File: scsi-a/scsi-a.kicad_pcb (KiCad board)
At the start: 2 copper layers, 99.1 x 99.1 mm, 18 parts, among them J1 Conn_02x25_Odd_Even, J3 Conn_02x08_Odd_Even, J4 Conn_02x08_Odd_Even, J5 DB25_Receptacle, J6 Conn_02x10_Counter_Clockwise, J7 Conn_02x10_Counter_Clockwise, Q1 BC547, U1 Z53C80003VSG, U2 74LS138, U3 74HC00

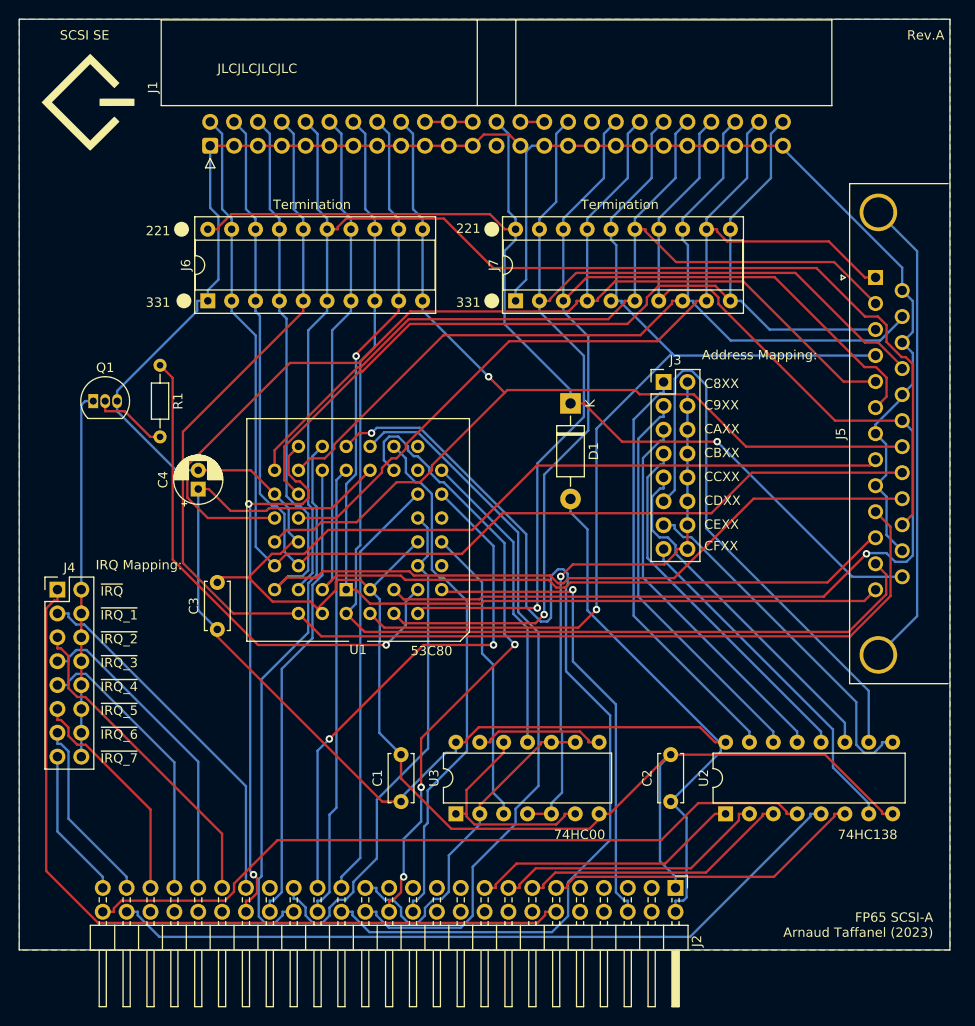
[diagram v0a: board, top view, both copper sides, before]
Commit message: Minimal change to fix SCSI CPU-Bus connection
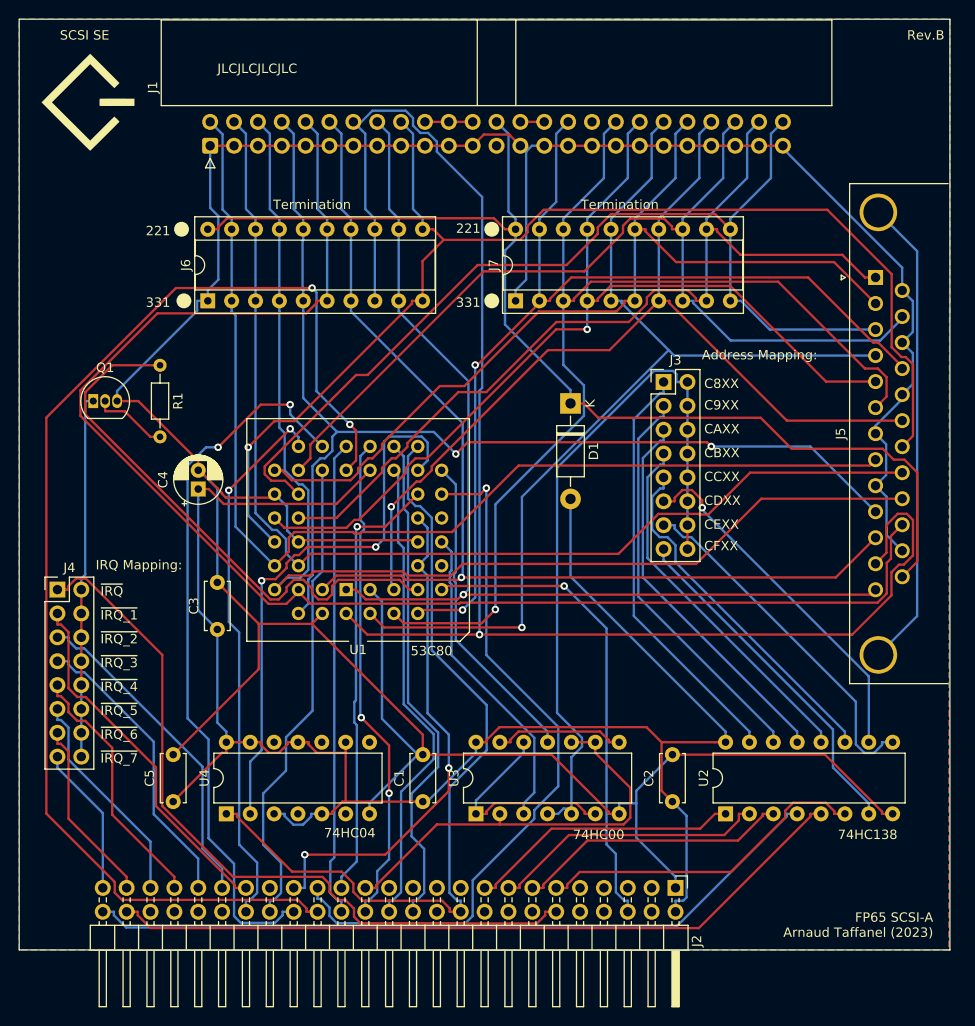
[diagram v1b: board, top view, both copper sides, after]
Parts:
- added C5: C, Capacitor_THT:C_Disc_D5.0mm_W2.5mm_P5.00mm, F.Cu at (118.0, 134.1)
- added U4: 74HC04, Package_DIP:DIP-14_W7.62mm, F.Cu at (123.6, 135.4)
- moved C1 2.32 mm to (144.6, 134.1)
- moved U3 2.13 mm to (150.2, 135.4)
- moved C2 0.18 mm to (171.1, 134.1)
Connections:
- U1 pad 18: /~{IOW} -> /R/~{W}
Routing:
- net /R/~{W}: track 0.00 -> 86.2 mm
- net /D3: track 48.5 -> 132.0 mm, vias 0 -> 2
- net /~{IOR}: track 0.00 -> 59.4 mm, vias 0 -> 2
- net /D4: track 108.8 -> 50.9 mm, vias 1 -> 0
- net /~{DB6}: track 118.2 -> 163.7 mm, vias 0 -> 1
- net GND: track 325.5 -> 367.5 mm
- net /~{SEL}: track 127.1 -> 99.4 mm
- net VCC: track 159.1 -> 186.0 mm
- net /D5: track 78.3 -> 52.8 mm, vias 0 -> 2
- net /~{CDXX}: track 63.1 -> 38.4 mm, vias 0 -> 1
- net /~{DB3}: track 143.2 -> 118.7 mm, vias 0 -> 2
- net /~{DBP}: track 109.7 -> 131.2 mm
- net /A1: track 56.3 -> 77.1 mm, vias 2 -> 1
- net /D2: track 57.9 -> 76.8 mm, vias 0 -> 2
- net /~{ACK}: track 121.0 -> 102.9 mm, vias 0 -> 1
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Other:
- board text added: "Rev.B"
- board text removed: "Rev.A"

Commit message: Fix DB footprint on SCSI-A and SIO-A
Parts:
- J5: footprint Connector_Dsub:DSUB-25_Female_Horizontal_P2.77x2.84mm_EdgePinOffset4.94mm_Housed_MountingHolesOffset7.48mm -> Connector_Dsub:DSUB-25_Female_Horizontal_P2.77x2.84mm_EdgePinOffset9.90mm_Housed_MountingHolesOffset11.32mm
- moved J5 4.93 mm to (187.8, 78.2)
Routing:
- net /D3: track 132.0 -> 50.3 mm, vias 2 -> 0
- net /~{DB0}: track 119.7 -> 179.5 mm
- net /D4: track 50.9 -> 106.2 mm, vias 0 -> 1
- net /~{DB6}: track 163.7 -> 112.9 mm, vias 1 -> 0
- net /~{DB1}: track 118.8 -> 146.9 mm, vias 0 -> 1
- net Net-(J3-Pin_10): track 78.1 -> 54.5 mm, vias 0 -> 1
- net /~{DBP}: track 131.2 -> 107.7 mm, vias 1 -> 2
- net /~{CCXX}: track 37.9 -> 61.3 mm
- net /A2: track 47.2 -> 65.1 mm
- net /D2: track 76.8 -> 94.2 mm, vias 2 -> 1
- net /A0: track 54.1 -> 70.2 mm, vias 2 -> 1
- net /I/~{O}: track 105.1 -> 91.2 mm
- net GND: track 367.5 -> 353.7 mm
- net /A1: track 77.1 -> 64.0 mm, vias 1 -> 2
- net /IRQ: track 59.2 -> 48.4 mm, vias 0 -> 1
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- removed copper zone on B.Cu, net GND
- removed copper zone on F.Cu, net GND
